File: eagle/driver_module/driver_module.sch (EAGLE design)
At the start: 14 parts, among them IC1 74ALS1035D, U1 DRV8825CARRIER

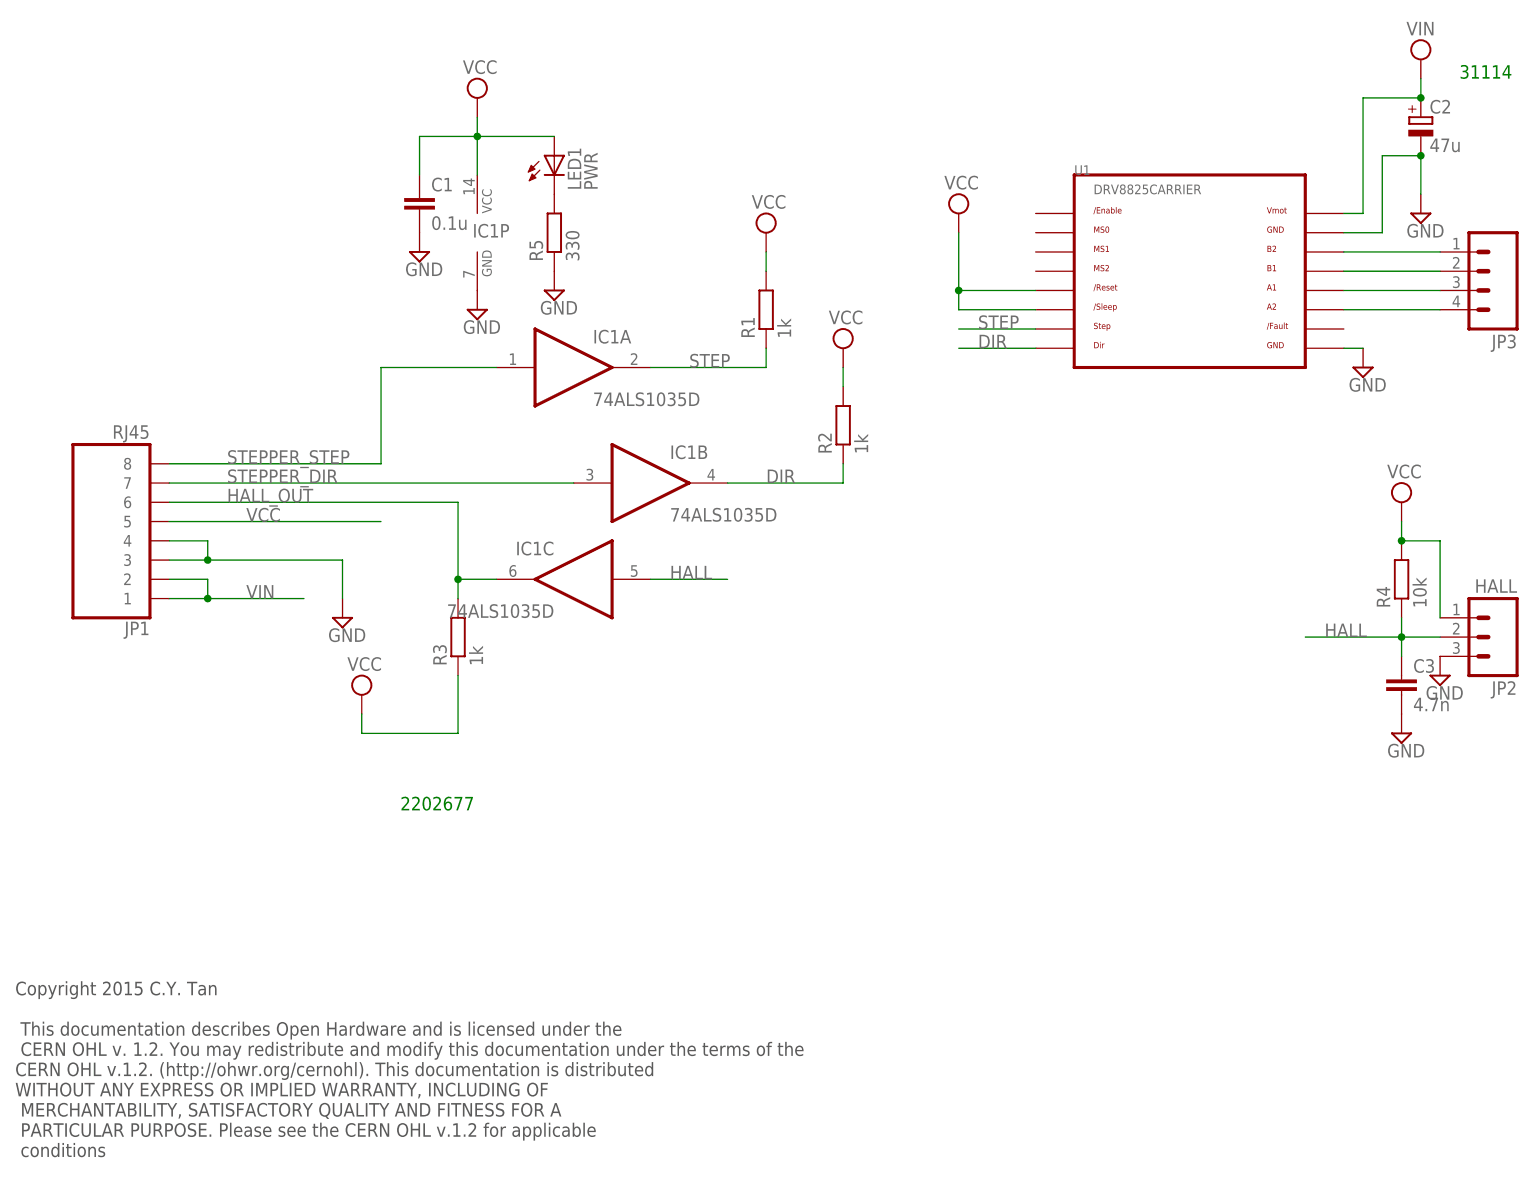
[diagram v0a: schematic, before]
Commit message: Updated eagle/driver_module schematic
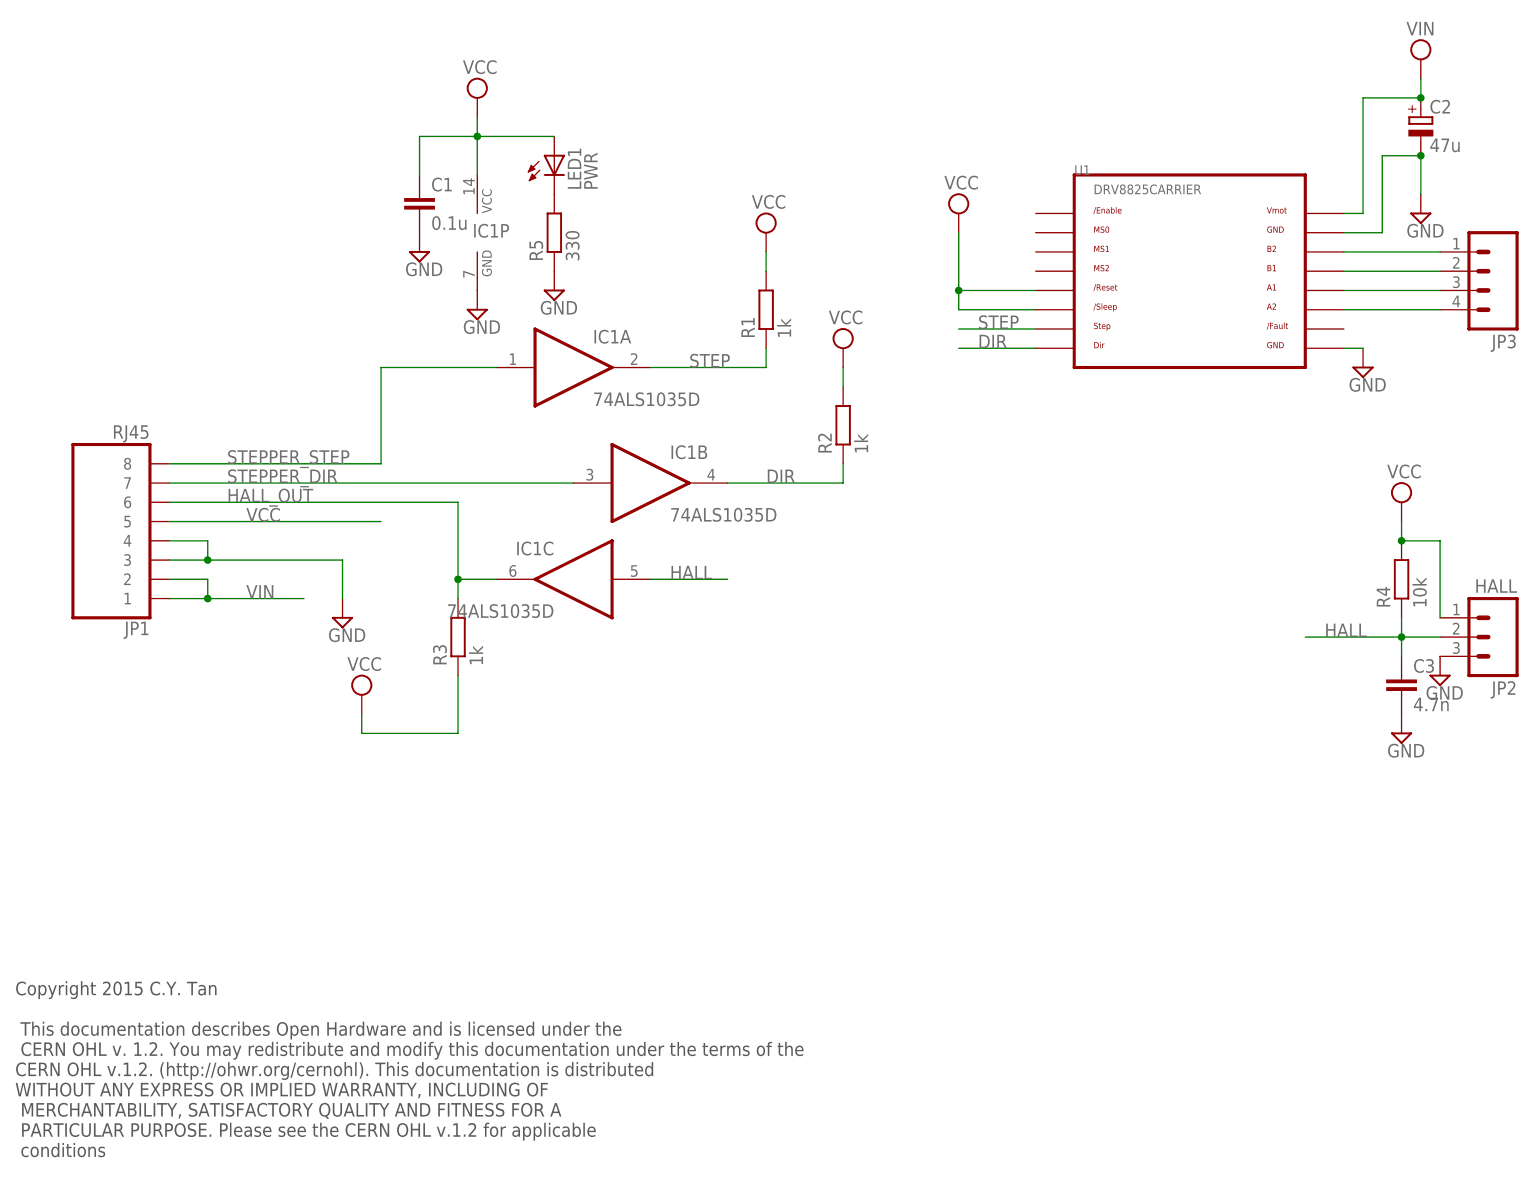
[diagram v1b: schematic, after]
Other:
- note removed: "2202677"
- note removed: "31114"
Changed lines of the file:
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@@
 <sheet>
 <plain>
-<text x="58.42" y="58.42" size="1.778" layer="91">2202677</text>
-<text x="198.12" y="154.94" size="1.778" layer="91">31114</text>
 <text x="7.62" y="12.7" size="1.778" layer="97">Copyright 2015 C.Y. Tan
  This documentation describes Open Hardware and is licensed under the
